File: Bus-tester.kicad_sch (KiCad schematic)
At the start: 79 parts, among them J1 POWER, J10 In_Reg, J11 Out_Reg, J12 POWER, J2 POWER, J3 C1_out, J4 C2_out, J5 C3_out, J6 C4_out, J7 Out_sw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

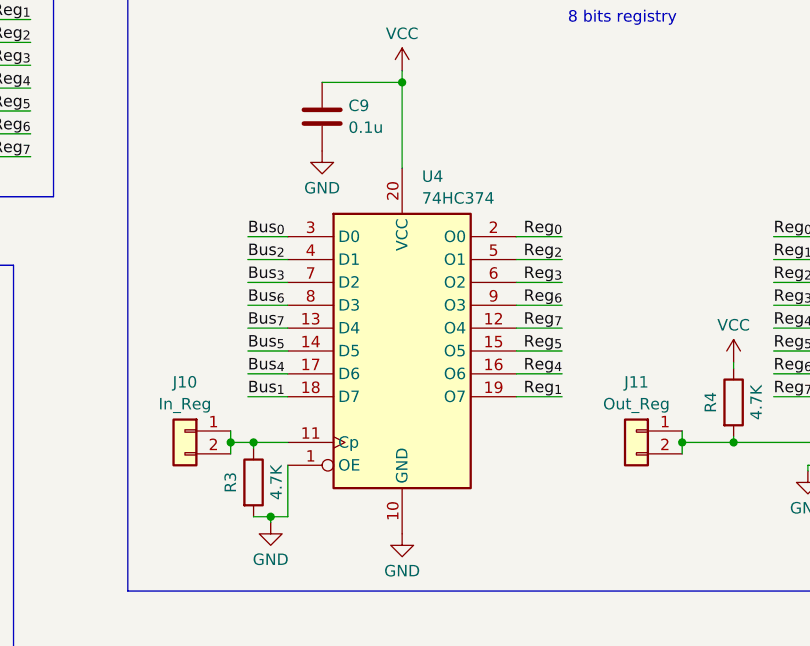
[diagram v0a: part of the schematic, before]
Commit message: change register chip ref for cleaner routing
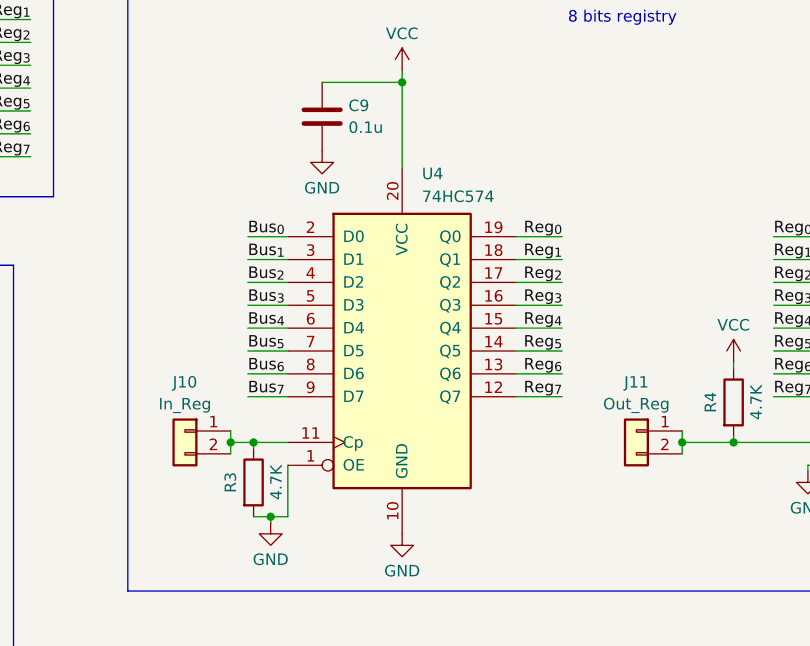
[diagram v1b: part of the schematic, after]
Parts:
- U4: value 74HC374 -> 74HC574; symbol 74xx:74HC374 -> 74xx:74HCT574
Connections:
- net Bus_{0}: now also U4.2 (D0); no longer U4.3 (D0)
- net Bus_{1}: now also U4.3 (D1); no longer U4.18 (D7)
- net Bus_{3}: now also U4.5 (D3); no longer U4.7 (D2)
- net Bus_{4}: now also U4.6 (D4); no longer U4.17 (D6)
- net Bus_{5}: now also U4.7 (D5); no longer U4.14 (D5)
- net Bus_{7}: now also U4.9 (D7); no longer U4.13 (D4)
- net Reg_{0}: now also U4.19 (Q0); no longer U4.2 (O0)
- net Reg_{1}: now also U4.18 (Q1); no longer U4.19 (O7)
- net Reg_{2}: now also U4.17 (Q2); no longer U4.5 (O1)
- net Reg_{3}: now also U4.16 (Q3); no longer U4.6 (O2)
- net Reg_{4}: now also U4.15 (Q4); no longer U4.16 (O6)
- net Reg_{5}: now also U4.14 (Q5); no longer U4.15 (O5)
- net Reg_{6}: now also U4.13 (Q6); no longer U4.9 (O3)
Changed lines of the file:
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@@
     (effects (font (size 1.27 1.27)) (justify right bottom))
   )
-  (label "Bus_{2}" (at 184.15 93.345 0) (fields_autoplaced)
+  (label "Bus_{1}" (at 184.15 93.345 0) (fields_autoplaced)
     (effects (font (size 1.27 1.27)) (justify left bottom))
   )
-  (label "Reg_{1}" (at 219.075 108.585 180) (fields_autoplaced)
+  (label "Reg_{7}" (at 219.075 108.585 180) (fields_autoplaced)
     (effects (font (size 1.27 1.27)) (justify right bottom))
   )
-  (label "Reg_{3}" (at 219.075 95.885 180) (fields_autoplaced)
+  (label "Reg_{2}" (at 219.075 95.885 180) (fields_autoplaced)
     (effects (font (size 1.27 1.27)) (justify right bottom))
   )
@@
     (effects (font (size 1.27 1.27)) (justify right bottom))
   )
-  (label "Bus_{3}" (at 184.15 95.885 0) (fields_autoplaced)
+  (label "Bus_{2}" (at 184.15 95.885 0) (fields_autoplaced)
     (effects (font (size 1.27 1.27)) (justify left bottom))
   )
-  (label "Reg_{2}" (at 219.075 93.345 180) (fields_autoplaced)
+  (label "Reg_{1}" (at 219.075 93.345 180) (fields_autoplaced)
     (effects (font (size 1.27 1.27)) (justify right bottom))
   )
@@
     (effects (font (size 1.27 1.27)) (justify left bottom))
   )
-  (label "Bus_{6}" (at 184.15 98.425 0) (fields_autoplaced)
+  (label "Bus_{3}" (at 184.15 98.425 0) (fields_autoplaced)
     (effects (font (size 1.27 1.27)) (justify left bottom))
   )
@@
     (effects (font (size 1.27 1.27)) (justify left bottom))
   )
-  (label "Reg_{7}" (at 219.075 100.965 180) (fields_autoplaced)
+  (label "Reg_{4}" (at 219.075 100.965 180) (fields_autoplaced)
     (effects (font (size 1.27 1.27)) (justify right bottom))
   )
@@
     (effects (font (size 1.27 1.27)) (justify left bottom))
   )
-  (label "Reg_{4}" (at 219.075 106.045 180) (fields_autoplaced)
+  (label "Reg_{6}" (at 219.075 106.045 180) (fields_autoplaced)
     (effects (font (size 1.27 1.27)) (justify right bottom))
   )
@@
     (effects (font (size 1.27 1.27)) (justify left bottom))
   )
-  (label "Bus_{7}" (at 184.15 100.965 0) (fields_autoplaced)
+  (label "Bus_{4}" (at 184.15 100.965 0) (fields_autoplaced)
     (effects (font (size 1.27 1.27)) (justify left bottom))
   )
@@
     (effects (font (size 1.27 1.27)) (justify left bottom))
   )
-  (label "Bus_{1}" (at 184.15 108.585 0) (fields_autoplaced)
+  (label "Bus_{7}" (at 184.15 108.585 0) (fields_autoplaced)
     (effects (font (size 1.27 1.27)) (justify left bottom))
   )
@@
     (effects (font (size 1.27 1.27)) (justify left bottom))
   )
-  (label "Bus_{4}" (at 184.15 106.045 0) (fields_autoplaced)
+  (label "Bus_{6}" (at 184.15 106.045 0) (fields_autoplaced)
     (effects (font (size 1.27 1.27)) (justify left bottom))
   )
@@
     (effects (font (size 1.27 1.27)) (justify right bottom))
   )
-  (label "Reg_{6}" (at 219.075 98.425 180) (fields_autoplaced)
+  (label "Reg_{3}" (at 219.075 98.425 180) (fields_autoplaced)
     (effects (font (size 1.27 1.27)) (justify right bottom))
   )
@@
     )
   )
-  (symbol (lib_id "74xx:74HC374") (at 201.295 103.505 0) (unit 1)
+  (symbol (lib_id "74xx:74HCT574") (at 201.295 103.505 0) (unit 1)
     (in_bom yes) (on_board yes) (dnp no) (fields_autoplaced)
-    (property "Reference" "U4" (at 203.4891 84.1207 0)
+    (property "Reference" "U4" (at 203.4891 83.82 0)
       (effects (font (size 1.27 1.27)) (justify left))
     )
-    (property "Value" "74HC374" (at 203.4891 86.5449 0)
+    (property "Value" "74HC574" (at 203.4891 86.36 0)
       (effects (font (size 1.27 1.27)) (justify left))
     )
@@
       (effects (font (size 1.27 1.27)) hide)
     )
-    (property "Datasheet" "https://www.ti.com/lit/ds/symlink/cd74hct374.pdf" (at 201.295 103.505 0)
+    (property "Datasheet" "http://www.ti.com/lit/gpn/sn74HCT574" (at 201.295 103.505 0)
       (effects (font (size 1.27 1.27)) hide)
     )

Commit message: change resistor arrays footprints
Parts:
- RN1, RN10, RN11, RN2, RN4, RN5, RN6, RN7, RN8, RN9: footprint Resistor_SMD:R_Array_Convex_4x1206 -> Resistor_SMD:R_Array_Convex_4x0603
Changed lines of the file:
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@@
       (effects (font (size 1.27 1.27)))
     )
-    (property "Footprint" "Resistor_SMD:R_Array_Convex_4x1206" (at 269.24 24.13 90)
+    (property "Footprint" "Resistor_SMD:R_Array_Convex_4x0603" (at 269.24 24.13 90)
       (effects (font (size 1.27 1.27)) hide)
     )
@@
       (effects (font (size 1.27 1.27)) (justify left))
     )
-    (property "Footprint" "Resistor_SMD:R_Array_Convex_4x1206" (at 39.878 172.085 90)
+    (property "Footprint" "Resistor_SMD:R_Array_Convex_4x0603" (at 39.878 172.085 90)
       (effects (font (size 1.27 1.27)) hide)
     )
@@
       (effects (font (size 1.27 1.27)) (justify left))
     )
-    (property "Footprint" "Resistor_SMD:R_Array_Convex_4x1206" (at 39.878 106.045 90)
+    (property "Footprint" "Resistor_SMD:R_Array_Convex_4x0603" (at 39.878 106.045 90)
       (effects (font (size 1.27 1.27)) hide)
     )
@@
       (effects (font (size 1.27 1.27)))
     )
-    (property "Footprint" "Resistor_SMD:R_Array_Convex_4x1206" (at 24.13 75.438 90)
+    (property "Footprint" "Resistor_SMD:R_Array_Convex_4x0603" (at 24.13 75.438 90)
       (effects (font (size 1.27 1.27)) hide)
     )
@@
       (effects (font (size 1.27 1.27)))
     )
-    (property "Footprint" "Resistor_SMD:R_Array_Convex_4x1206" (at 269.24 39.37 90)
+    (property "Footprint" "Resistor_SMD:R_Array_Convex_4x0603" (at 269.24 39.37 90)
       (effects (font (size 1.27 1.27)) hide)
     )
@@
       (effects (font (size 1.27 1.27)))
     )
-    (property "Footprint" "Resistor_SMD:R_Array_Convex_4x1206" (at 237.49 55.88 90)
+    (property "Footprint" "Resistor_SMD:R_Array_Convex_4x0603" (at 237.49 55.88 90)
       (effects (font (size 1.27 1.27)) hide)
     )
@@
       (effects (font (size 1.27 1.27)))
     )
-    (property "Footprint" "Resistor_SMD:R_Array_Convex_4x1206" (at 237.49 40.64 90)
+    (property "Footprint" "Resistor_SMD:R_Array_Convex_4x0603" (at 237.49 40.64 90)
       (effects (font (size 1.27 1.27)) hide)
     )
@@
       (effects (font (size 1.27 1.27)))
     )
-    (property "Footprint" "Resistor_SMD:R_Array_Convex_4x1206" (at 139.7 188.595 90)
+    (property "Footprint" "Resistor_SMD:R_Array_Convex_4x0603" (at 139.7 188.595 90)
       (effects (font (size 1.27 1.27)) hide)
     )
@@
       (effects (font (size 1.27 1.27)))
     )
-    (property "Footprint" "Resistor_SMD:R_Array_Convex_4x1206" (at 203.835 40.64 90)
+    (property "Footprint" "Resistor_SMD:R_Array_Convex_4x0603" (at 203.835 40.64 90)
       (effects (font (size 1.27 1.27)) hide)
     )
@@
       (effects (font (size 1.27 1.27)))
     )
-    (property "Footprint" "Resistor_SMD:R_Array_Convex_4x1206" (at 203.835 55.88 90)
+    (property "Footprint" "Resistor_SMD:R_Array_Convex_4x0603" (at 203.835 55.88 90)
       (effects (font (size 1.27 1.27)) hide)
     )
@@
       (effects (font (size 1.27 1.27)))
     )
-    (property "Footprint" "Resistor_SMD:R_Array_Convex_4x1206" (at 24.13 174.498 90)
+    (property "Footprint" "Resistor_SMD:R_Array_Convex_4x0603" (at 24.13 174.498 90)
       (effects (font (size 1.27 1.27)) hide)
     )
@@
       (effects (font (size 1.27 1.27)) (justify left))
     )
-    (property "Footprint" "Resistor_SMD:R_Array_Convex_4x1206" (at 39.878 73.025 90)
+    (property "Footprint" "Resistor_SMD:R_Array_Convex_4x0603" (at 39.878 73.025 90)
       (effects (font (size 1.27 1.27)) hide)
     )
@@
       (effects (font (size 1.27 1.27)))
     )
-    (property "Footprint" "Resistor_SMD:R_Array_Convex_4x1206" (at 139.7 177.165 90)
+    (property "Footprint" "Resistor_SMD:R_Array_Convex_4x0603" (at 139.7 177.165 90)
       (effects (font (size 1.27 1.27)) hide)
     )
@@
       (effects (font (size 1.27 1.27)))
     )
-    (property "Footprint" "Resistor_SMD:R_Array_Convex_4x1206" (at 24.13 141.478 90)
+    (property "Footprint" "Resistor_SMD:R_Array_Convex_4x0603" (at 24.13 141.478 90)
       (effects (font (size 1.27 1.27)) hide)
     )
@@
       (effects (font (size 1.27 1.27)) (justify left))
     )
-    (property "Footprint" "Resistor_SMD:R_Array_Convex_4x1206" (at 39.878 139.065 90)
+    (property "Footprint" "Resistor_SMD:R_Array_Convex_4x0603" (at 39.878 139.065 90)
       (effects (font (size 1.27 1.27)) hide)
     )
@@
       (effects (font (size 1.27 1.27)))
     )
-    (property "Footprint" "Resistor_SMD:R_Array_Convex_4x1206" (at 24.13 108.458 90)
+    (property "Footprint" "Resistor_SMD:R_Array_Convex_4x0603" (at 24.13 108.458 90)
       (effects (font (size 1.27 1.27)) hide)
     )
